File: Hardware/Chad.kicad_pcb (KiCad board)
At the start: 4 copper layers, 30 x 60 mm, 101 parts, among them J1 RBUS, J2 GPIO Breakout, J3 ServoCH2, J4 ServoCH2, J5 USB_C_Receptacle_USB2.0, U1 ESP32-S3, U2 SN65HVD230, U3 LM66200DRLR, U4 MAX77827AEFD+T, U5 SC4215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

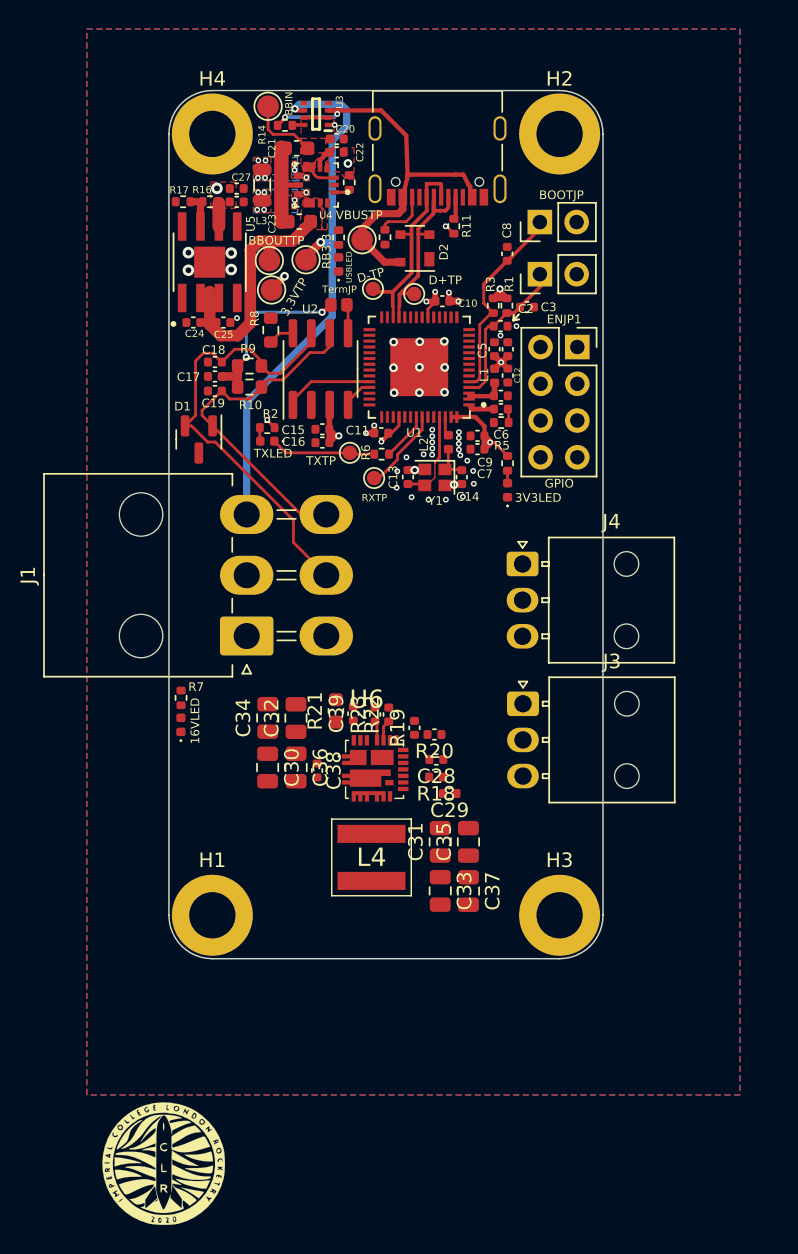
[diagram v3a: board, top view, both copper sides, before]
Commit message: on the verge of being complete, also updated to kicad 7
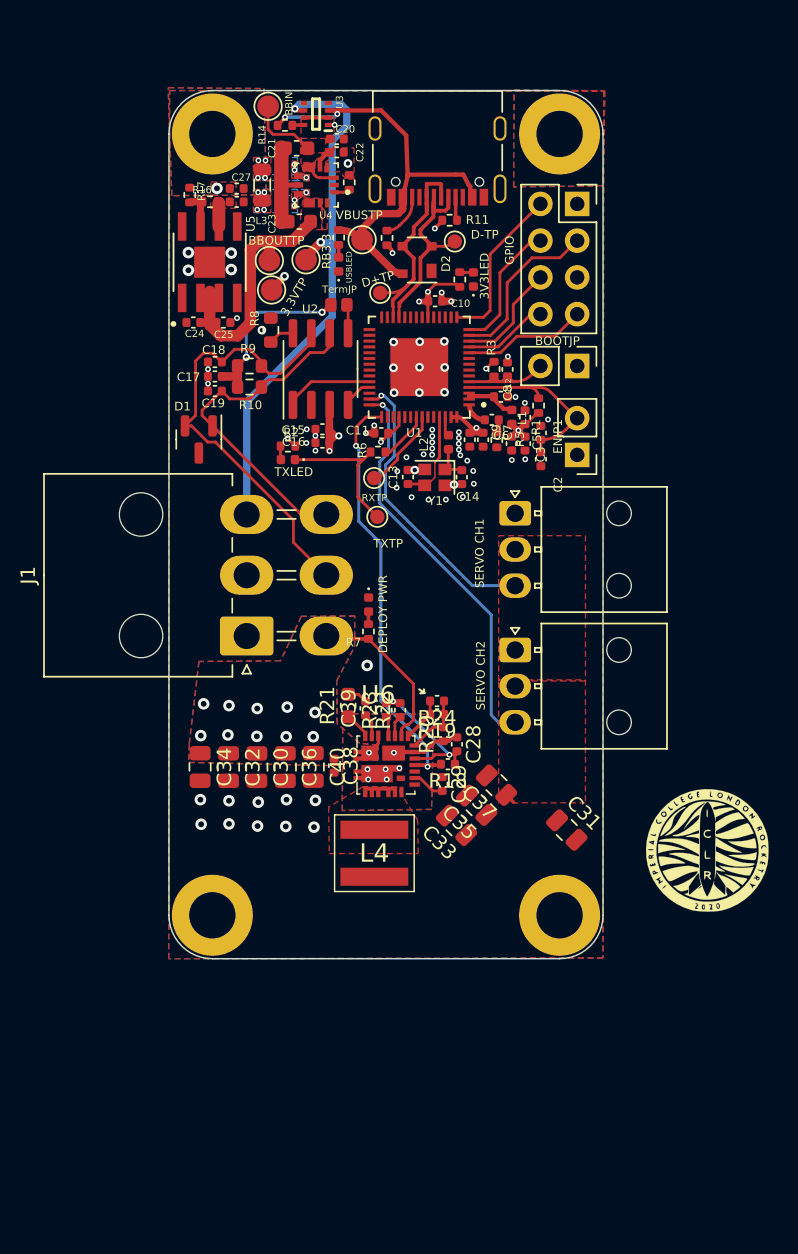
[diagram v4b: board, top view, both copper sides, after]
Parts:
- added C40: 22uF, Capacitor_SMD:C_0805_2012Metric, F.Cu at (42.0, 88.8)
- added R24: 294k, Capacitor_SMD:C_0402_1005Metric, F.Cu at (50.5, 84.3)
- J3: renamed from J4; value ServoCH2 -> ServoCH1
- R19: value RFBH -> 130k
- R20: value RFBL -> 10k
- moved LOGO1 43.4 mm to (69.2, 94.6)
- moved 12VLED1 15.4 mm to (45.8, 77.6), turned to -90 degrees
- moved 3V3LED1 14.8 mm to (53.0, 55.1)
- moved R7 13.7 mm to (45.8, 79.5), turned to 90 degrees
- moved R4 13.1 mm to (52.1, 55.1), turned to -90 degrees
- moved ENJUMPER1 12.8 mm to (60.2, 67.3), turned to 180 degrees
- moved BOOTJUMPER1 10.3 mm to (60.2, 61.1), turned to -90 degrees
- moved J2 9.89 mm to (60.2, 49.9)
- moved C2 9.61 mm to (57.7, 67.6), turned to -90 degrees
- moved C31 8.79 mm to (59.5, 93.2), turned to -45 degrees
- moved C3 8.75 mm to (57.7, 65.8), turned to -90 degrees
- moved C8 7.99 mm to (55.4, 61.4), turned to -90 degrees
- moved C37 7.57 mm to (54.6, 90.1), turned to 135 degrees
- moved R1 7.25 mm to (57.5, 63.9), turned to 90 degrees
- moved C5 6.86 mm to (56.6, 66.5), turned to -90 degrees
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- renumbered J3 to J4
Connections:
- BOOTJUMPER1 pad 1: /BOOT -> GND
- BOOTJUMPER1 pad 2: GND -> /BOOT
- C28 pad 1: GNDA -> GND
- C3 pad 1: /CHIP_PU -> GND
- C3 pad 2: GND -> /CHIP_PU
- C38 pad 2: GNDA -> GND
- C8 pad 1: /BOOT -> GND
- C8 pad 2: GND -> /BOOT
- ENJUMPER1 pad 1: /CHIP_PU -> GND
- ENJUMPER1 pad 2: GND -> /CHIP_PU
- J2 pad 1: /GPIO0 -> GND
- J2 pad 2: +3V3 -> /GPIO0
- J2 pad 3: GND -> /GPIO1
- J2 pad 4: /GPIO1 -> /GPIO2
- J2 pad 5: /GPIO2 -> +3V3
- J3 pad 3: /Servo2PWM -> /Servo1PWM
- J4 pad 1: (no net) -> GND
- J4 pad 2: (no net) -> +6V
- J4 pad 3: (no net) -> /Servo2PWM
- R18 pad 2: Net-(R18-Pad2) -> /BuckPGOOD
- R20 pad 1: GNDA -> GND
- U1 pad 10: unconnected-(U1-Pad10) -> /GPIO4
- U1 pad 11: unconnected-(U1-Pad11) -> /GPIO5
- U1 pad 12: unconnected-(U1-Pad12) -> /GPIO3
- U1 pad 13: unconnected-(U1-Pad13) -> /GPIO1
- U1 pad 14: unconnected-(U1-Pad14) -> /GPIO2
- U1 pad 15: unconnected-(U1-Pad15) -> /GPIO0
- U1 pad 41: unconnected-(U1-Pad41) -> /Servo1PWM
- U1 pad 42: unconnected-(U1-Pad42) -> /Servo2PWM
- U1 pad 43: unconnected-(U1-Pad43) -> /BuckPGOOD
- U6 pad 14: Net-(R18-Pad2) -> /BuckPGOOD
- U6 pad 16: GNDA -> GND
- U6 pad 25: GNDA -> GND
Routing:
- net /BuckPGOOD: track 0.00 -> 30.9 mm, vias 0 -> 2
- net /Servo2PWM: track 0.00 -> 27.8 mm, vias 0 -> 1
- net /Servo1PWM: track 0.00 -> 20.2 mm, vias 0 -> 1
- net +12V: track 0.00 -> 12.9 mm, vias 0 -> 11
- net /GPIO1: track 0.00 -> 11.6 mm
- net /GPIO0: track 0.00 -> 11.3 mm
- net /buckC/VDD: track 0.00 -> 10.3 mm, vias 0 -> 2
- net /GPIO2: track 0.00 -> 9.18 mm
- net /GPIO4: track 0.00 -> 8.58 mm
- net /GPIO3: track 0.00 -> 7.50 mm
- net /BOOT: track 15.1 -> 8.46 mm
- net GND: track 9.95 -> 15.9 mm, vias 46 -> 75
- net /GPIO5: track 0.00 -> 5.87 mm
- net /buckC/FB: track 0.00 -> 4.34 mm
- net +6V: track 0.00 -> 3.79 mm
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- added copper zone on B.Cu, net +12V
- added copper zone on F.Cu, net +12V
- added copper zone on F.Cu, net +6V
- added copper zone on F.Cu, net /buckC/SW

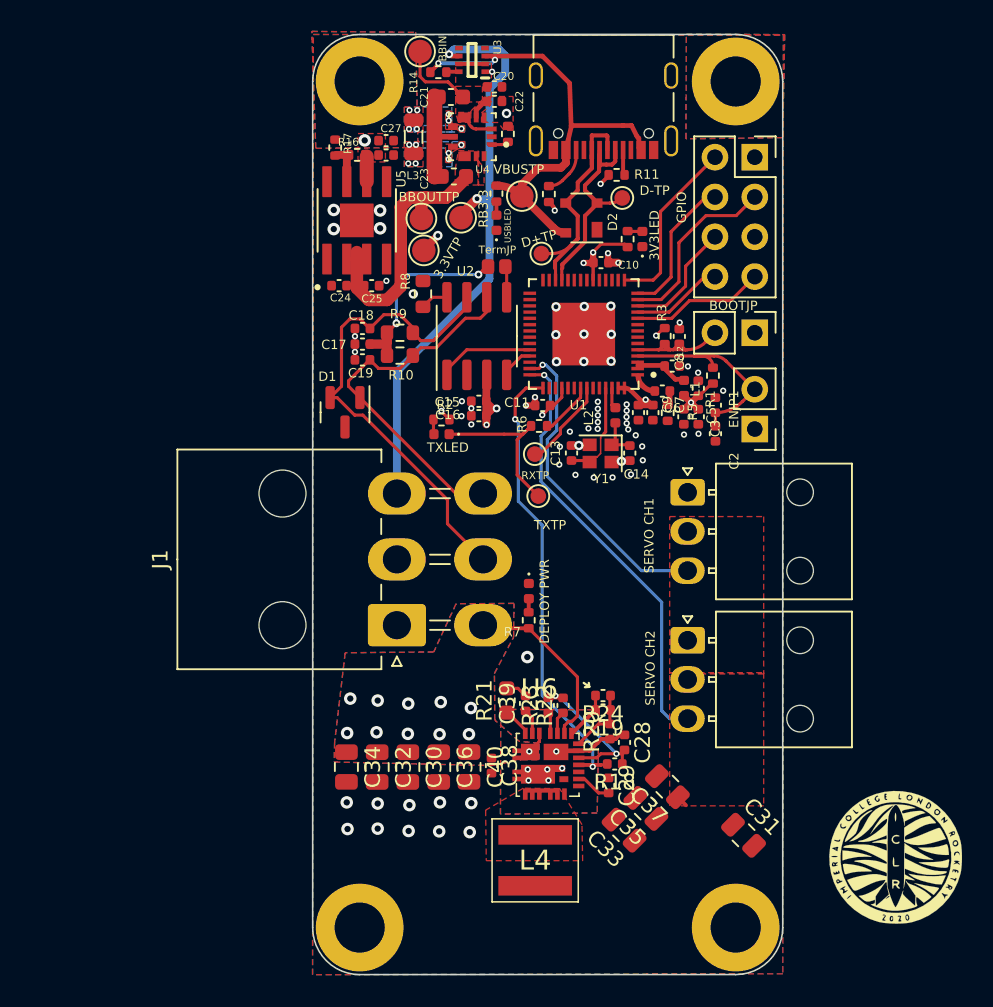
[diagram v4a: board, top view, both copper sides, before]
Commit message: all the important stuff routed, only back gfx and via stitch left
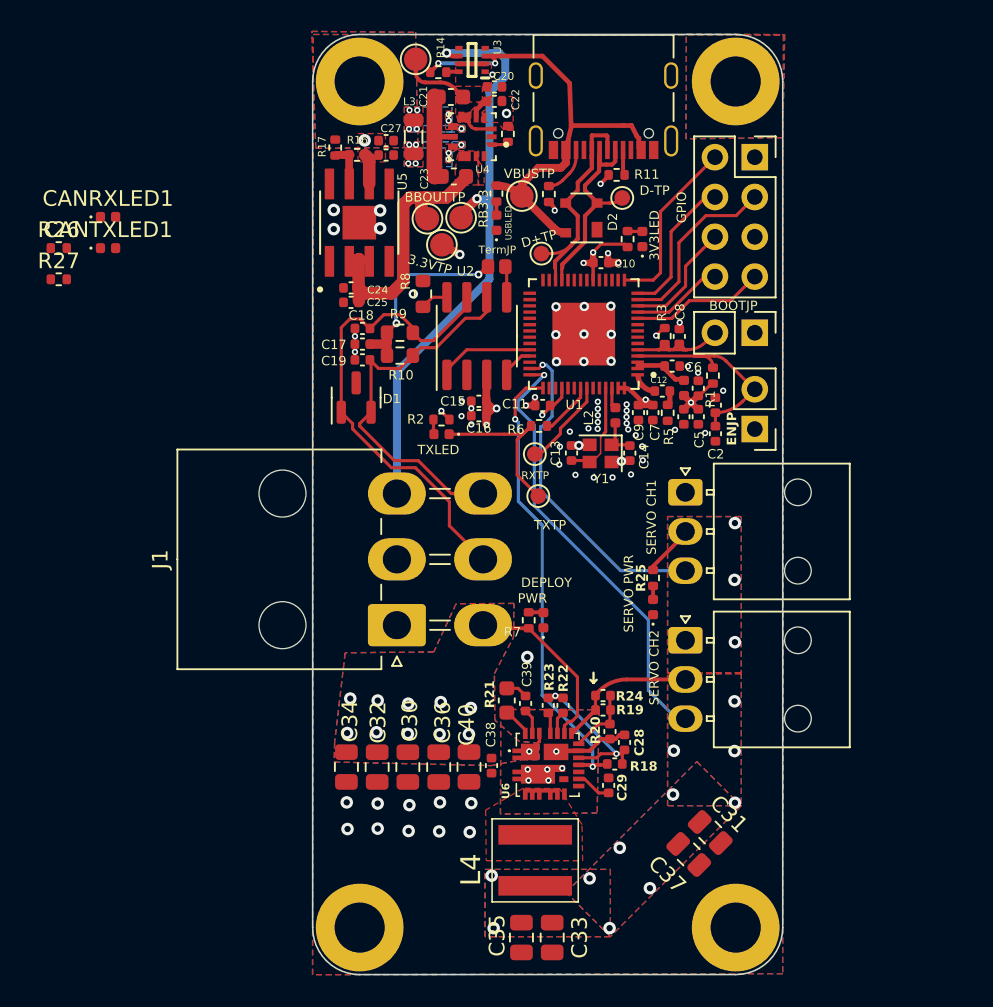
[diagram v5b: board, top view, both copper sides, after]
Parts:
- added CANRXLED1: CANRXLED, LED_SMD:LED_0402_1005Metric, F.Cu at (18.9, 53.7)
- added CANTXLED1: CANTXLED, LED_SMD:LED_0402_1005Metric, F.Cu at (18.9, 55.7)
- added R25: 1k, Resistor_SMD:R_0402_1005Metric, F.Cu at (53.7, 76.8)
- added R26: 470, Resistor_SMD:R_0402_1005Metric, F.Cu at (15.8, 55.7)
- added R27: 470, Resistor_SMD:R_0402_1005Metric, F.Cu at (15.8, 57.7)
- added SERVOLED1: 6V_LED, LED_SMD:LED_0402_1005Metric, F.Cu at (53.7, 78.6)
- LOGO1: moved to B.Cu
- moved LOGO1 28.1 mm to (94.9, 83.2), turned to 180 degrees
- moved C35 11.4 mm to (45.3, 99.7), turned to -90 degrees
- moved C33 8.25 mm to (47.3, 99.7), turned to -90 degrees
- moved C37 4.54 mm to (56.0, 94.4), turned to -45 degrees
- moved C31 2.13 mm to (57.4, 93.0)
- moved 12VLED1 2.08 mm to (46.7, 79.5), turned to 90 degrees
- moved C25 1.69 mm to (34.5, 59.2), turned to 180 degrees
- moved TP6 1.21 mm to (40.2, 55.5), turned to -75 degrees
- moved D1 1.18 mm to (34.8, 65.3), turned to 90 degrees
- moved C24 0.78 mm to (34.5, 58.3)
- moved TP4 0.57 mm to (38.6, 43.7)
- moved TP8 0.39 mm to (39.3, 53.9)
- moved U5 0.22 mm to (35.0, 54.1)
- moved J3 0.14 mm to (55.8, 71.3)
- moved J4 0.14 mm to (55.8, 80.8)
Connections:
- D1 pad 1: /CAN- -> /CAN+
- D1 pad 2: /CAN+ -> /CAN-
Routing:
- net +6V: track 3.79 -> 12.1 mm, vias 0 -> 14
- net /Servo2PWM: track 27.8 -> 29.1 mm
- net Net-(SERVOLED1-A): track 0.00 -> 0.87 mm
- net /Power/FBIn: track 2.61 -> 3.27 mm
- net /CAN-: track 23.8 -> 24.3 mm
- net GND: track 15.9 -> 15.4 mm, vias 75 -> 74
- added copper zone on B.Cu, net +6V

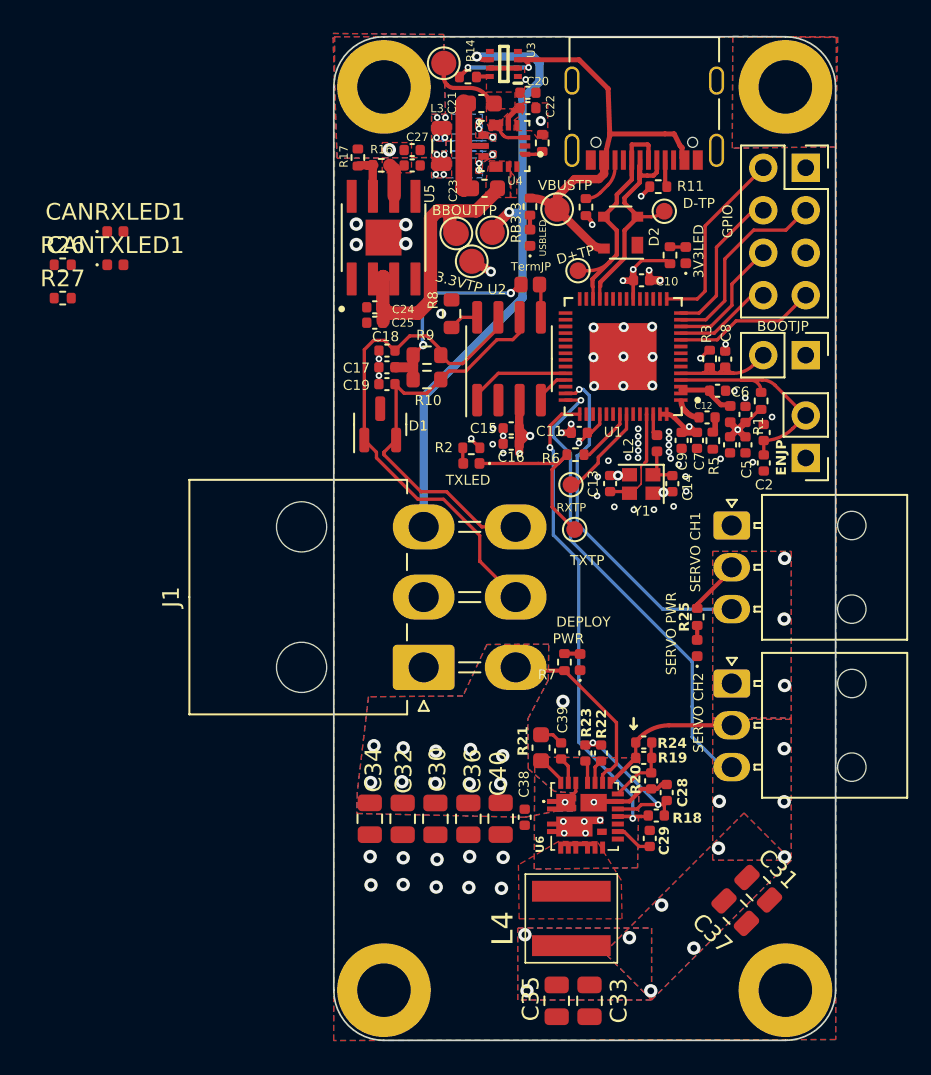
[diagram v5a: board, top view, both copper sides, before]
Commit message: added DNP capacitors, via fencing. still left: reduce number of vias
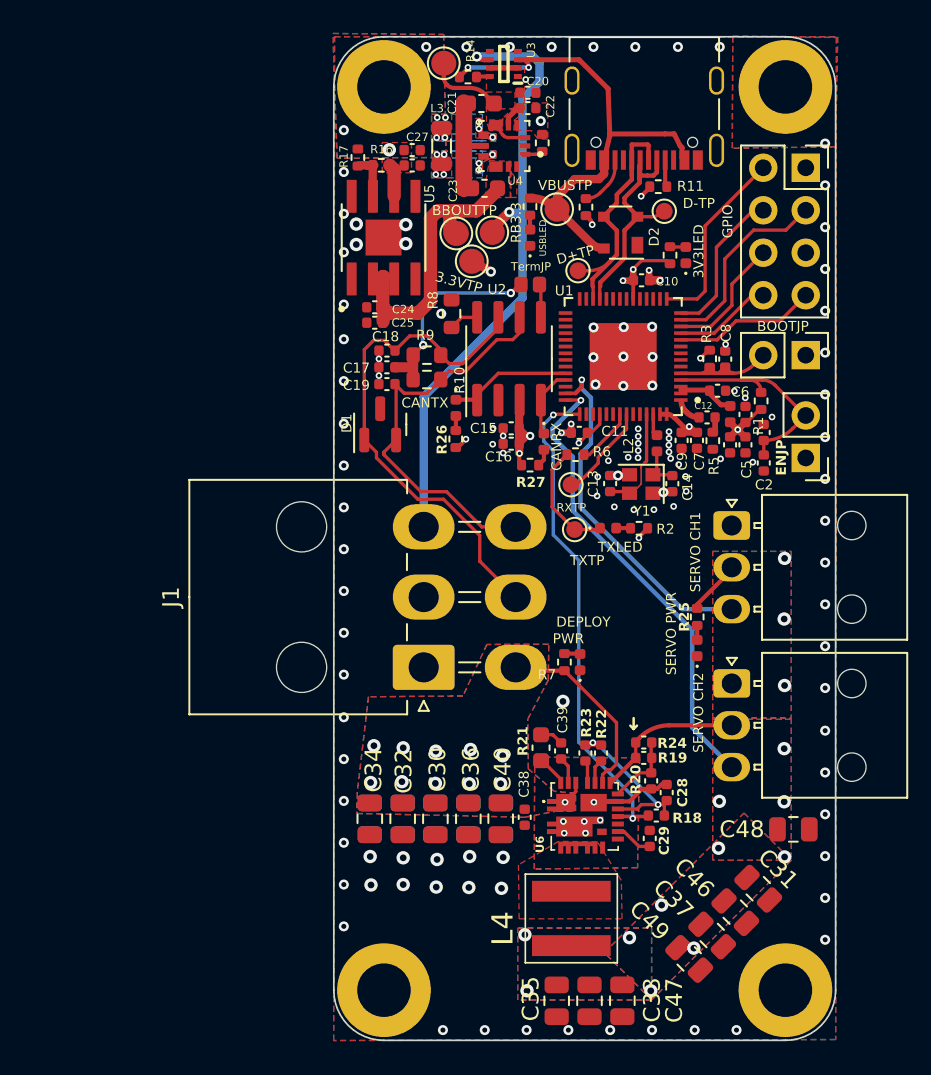
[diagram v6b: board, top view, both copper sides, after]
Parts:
- added C41: DNP, Capacitor_SMD:C_0805_2012Metric, B.Cu at (34.1, 88.8)
- added C42: DNP, Capacitor_SMD:C_0805_2012Metric, B.Cu at (36.1, 88.8)
- added C43: DNP, Capacitor_SMD:C_0805_2012Metric, B.Cu at (38.1, 88.8)
- added C44: DNP, Capacitor_SMD:C_0805_2012Metric, B.Cu at (40.0, 88.8)
- added C45: DNP, Capacitor_SMD:C_0805_2012Metric, B.Cu at (42.0, 88.8)
- added C46: DNP, Capacitor_SMD:C_0805_2012Metric, F.Cu at (54.6, 95.8)
- added C47: DNP, Capacitor_SMD:C_0805_2012Metric, F.Cu at (49.3, 99.7)
- added C48: DNP, Capacitor_SMD:C_0805_2012Metric, F.Cu at (59.5, 89.5)
- added C49: DNP, Capacitor_SMD:C_0805_2012Metric, F.Cu at (53.2, 97.2)
- added G***: LOGO, LOGO, B.Cu at (46.2, 57.7)
- moved LOGO1 45.6 mm to (49.4, 81.5)
- moved R27 29.7 mm to (43.7, 67.7)
- moved CANRXLED1 28.5 mm to (44.6, 66.3), turned to -90 degrees
- moved R26 25.7 mm to (39.3, 66.1), turned to 90 degrees
- moved CANTXLED1 22.1 mm to (39.3, 64.3), turned to -90 degrees
- moved R2 11.1 mm to (50.2, 71.5)
- moved TXLED1 9.04 mm to (48.4, 71.5), turned to 0 degrees
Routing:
- net /TXD: track 10.9 -> 7.69 mm
- net /CAN_RX: track 2.13 -> 4.20 mm
- net +3V3: track 26.5 -> 28.2 mm, vias 11 -> 12
- net /CAN_TX: track 6.16 -> 7.44 mm
- net Net-(CANRXLED1-A): track 0.00 -> 1.05 mm
- net Net-(CANTXLED1-A): track 0.00 -> 0.88 mm
- net /BuckPGOOD: track 30.9 -> 31.5 mm
- net /Servo1PWM: track 20.7 -> 21.2 mm
- net GND: vias 74 -> 130
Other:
- board text added: "C - CAN H - H-Bridge A - Actuator D - DC"
- board text added: "C.H.A.D-v2"
- board text added: "Designed By Andrei Paduraru Electronics and Payload 2023"
